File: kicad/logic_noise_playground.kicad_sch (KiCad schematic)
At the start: 39 parts, among them J1 JACK_TRS_6PINS, P1 CONN_02X03, P10 CONN_01X03, P11 CONN_01X05, P12 CONN_02X04, P13 CONN_01X03, P14 CONN_01X02, P15 CONN_02X08, P16 CONN_01X04, P17 CONN_02X04, P19 CONN_01X02, P2 CONN_01X02, P20 CONN_01X06, P21 CONN_02X03, P22 CONN_02X03, P23 CONN_01X02, P24 CONN_02X01, P25 CONN_01X02, P26 CONN_02X12, P27 CONN_01X02, P28 CONN_01X02, P29 CONN_01X02, P3 CONN_02X02, P30 CONN_01X02, P31 CONN_01X02, P32 CONN_01X03, P36 CONN_01X04, P37 CONN_02X01, P4 CONN_02X06, P40 CONN_01X02, P5 CONN_02X02, P6 4017 Outs, P7 CONN_01X08, P8 CONN_02X03, P9 CONN_01X08

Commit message: update connectors
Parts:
- RR1: manf# (none) -> 4610X-101-104LF
- RR2: manf# (none) -> 4610X-101-105LF
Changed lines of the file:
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@@
 			)
 		)
-		(property "manf#" ""
+		(property "manf#" "4610X-101-104LF "
 			(at 175.26 43.18 0)
 			(effects
@@
 			)
 		)
-		(property "manf#" ""
+		(property "manf#" "4610X-101-105LF "
 			(at 175.26 66.04 0)
 			(effects

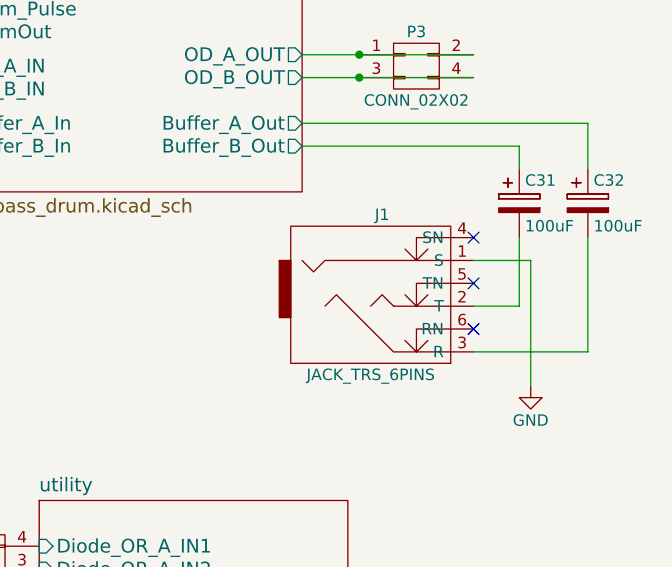
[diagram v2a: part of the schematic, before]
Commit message: update stereo TRSS connector
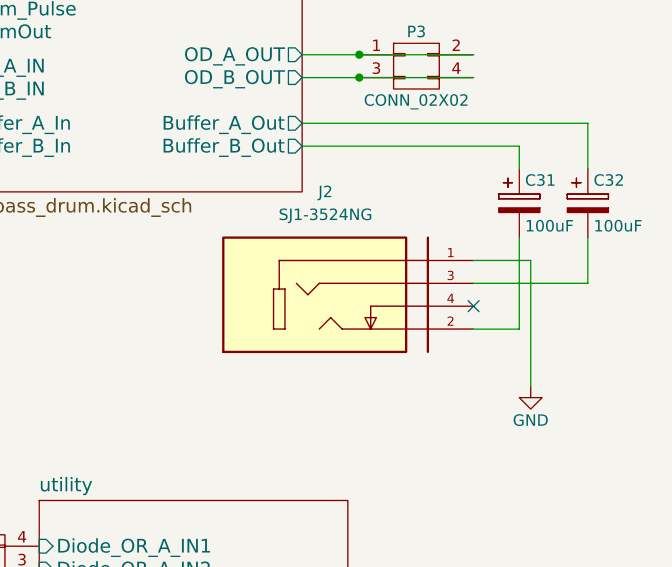
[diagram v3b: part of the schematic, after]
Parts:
- removed J1: JACK_TRS_6PINS, elliot:stereo_jack, symbol logic_noise_playground-rescue:JACK_TRS_6PINS
- added J2: SJ1-3524NG, logic_noise:CUI_SJ1-3524NG, symbol logic_noise:SJ1-3524NG
- C31, C32: manf# (none) -> RPA0609101M025B
- P1, P10, P11, P12, P13, P14, P15, P16, P17, P19, P2, P20, P21, P22, P23, P24, P25, P26, P27, P28, P29, P3, P30, P31, P32, P36, P37, P4, P40, P5, P6, P7, P8, P9: manf# (none) -> Pines
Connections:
- net GND: now also J2.1
- net at C31.2: now also J2.2
- net at C32.2: now also J2.3
- no-connect marks 3 -> 1

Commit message: update BOM
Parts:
- J2: manf# Pines -> SJ1-3524NG
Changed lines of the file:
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@@
 			)
 		)
-		(property "manf#" "Pines"
+		(property "manf#" "SJ1-3524NG"
 			(at 248.92 66.04 0)
 			(effects

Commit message: update to kicad 9, add some comments and circuit changes
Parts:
- C31, C32, J2, P1, P10, P11, P12, P13, P14, P15, P16, P17, P19, P2, P20, P21, P22, P23, P24, P25, P26, P27, P28, P29, P3, P30, P31, P32, P36, P37, P4, P40, P5, P6, P7, P8, P9, RR1, RR2: Orden (none) -> 99
